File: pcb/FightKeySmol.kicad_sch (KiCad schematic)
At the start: 14 parts

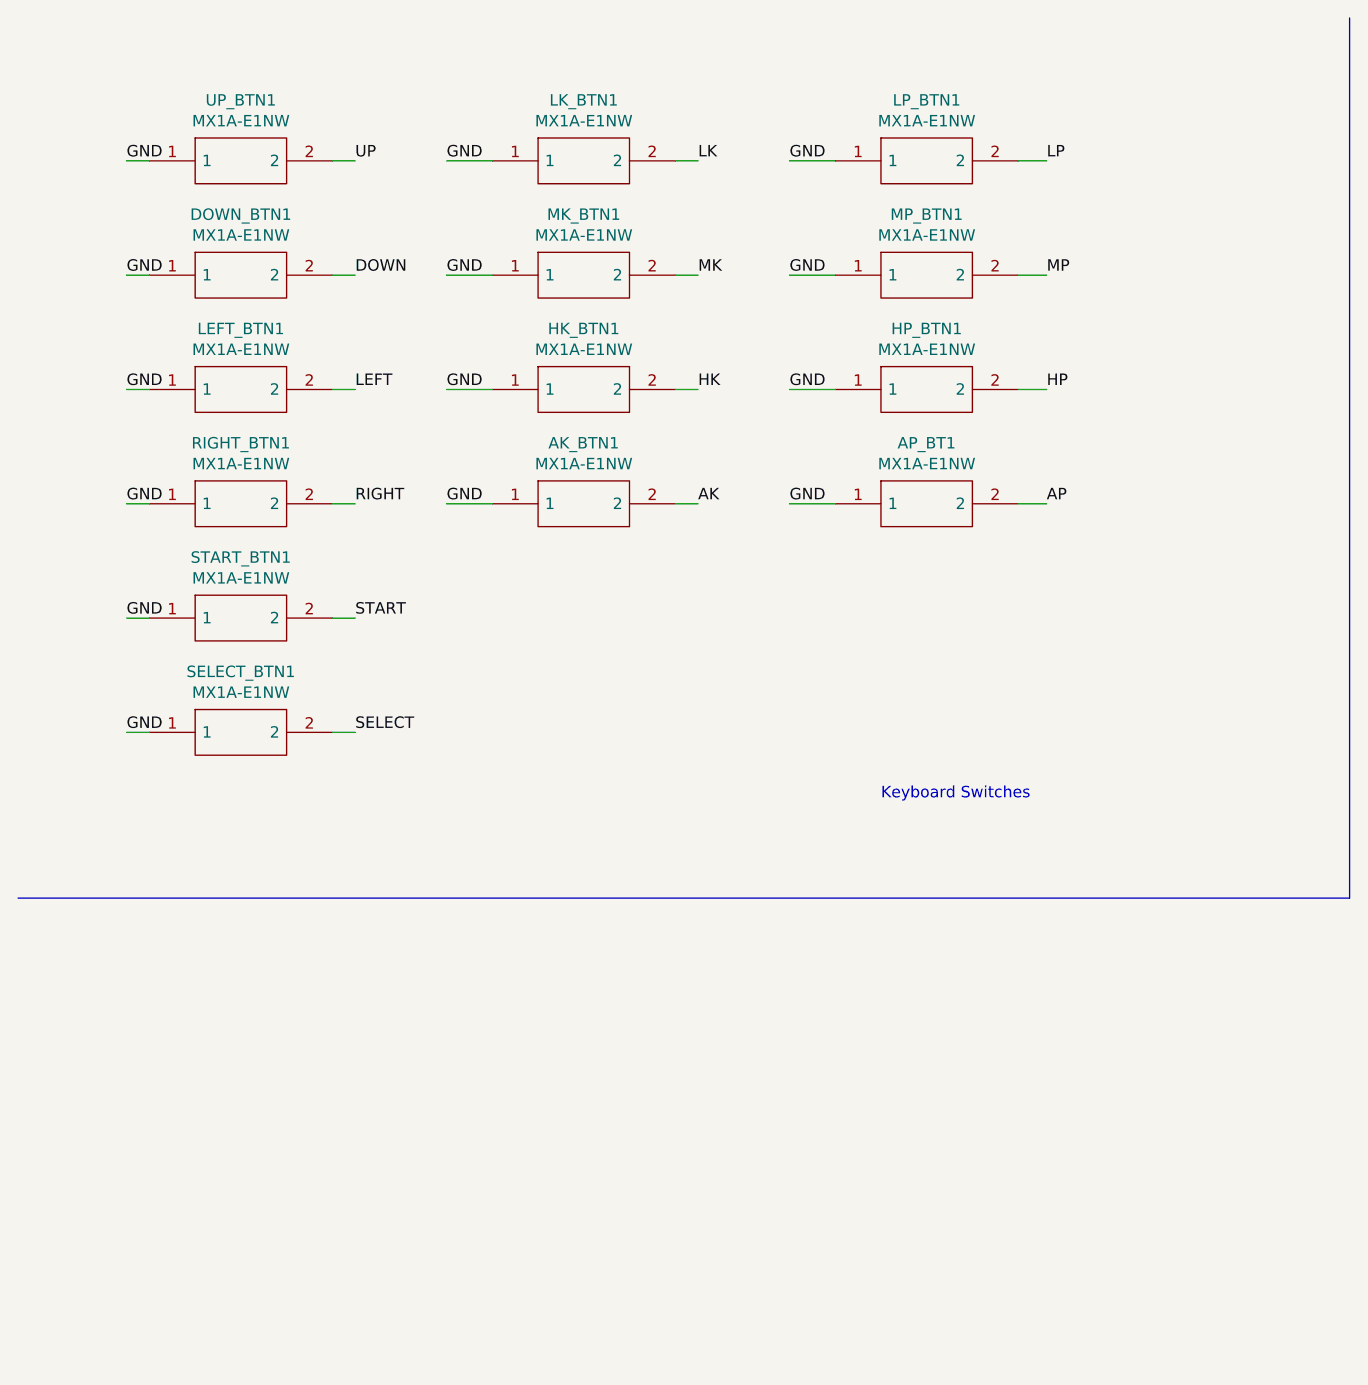
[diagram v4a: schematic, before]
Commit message: kicad_sch: implement USB/Power circuit
Signed-off-by: Dylan Turner <dylantdmt@gmail.com>
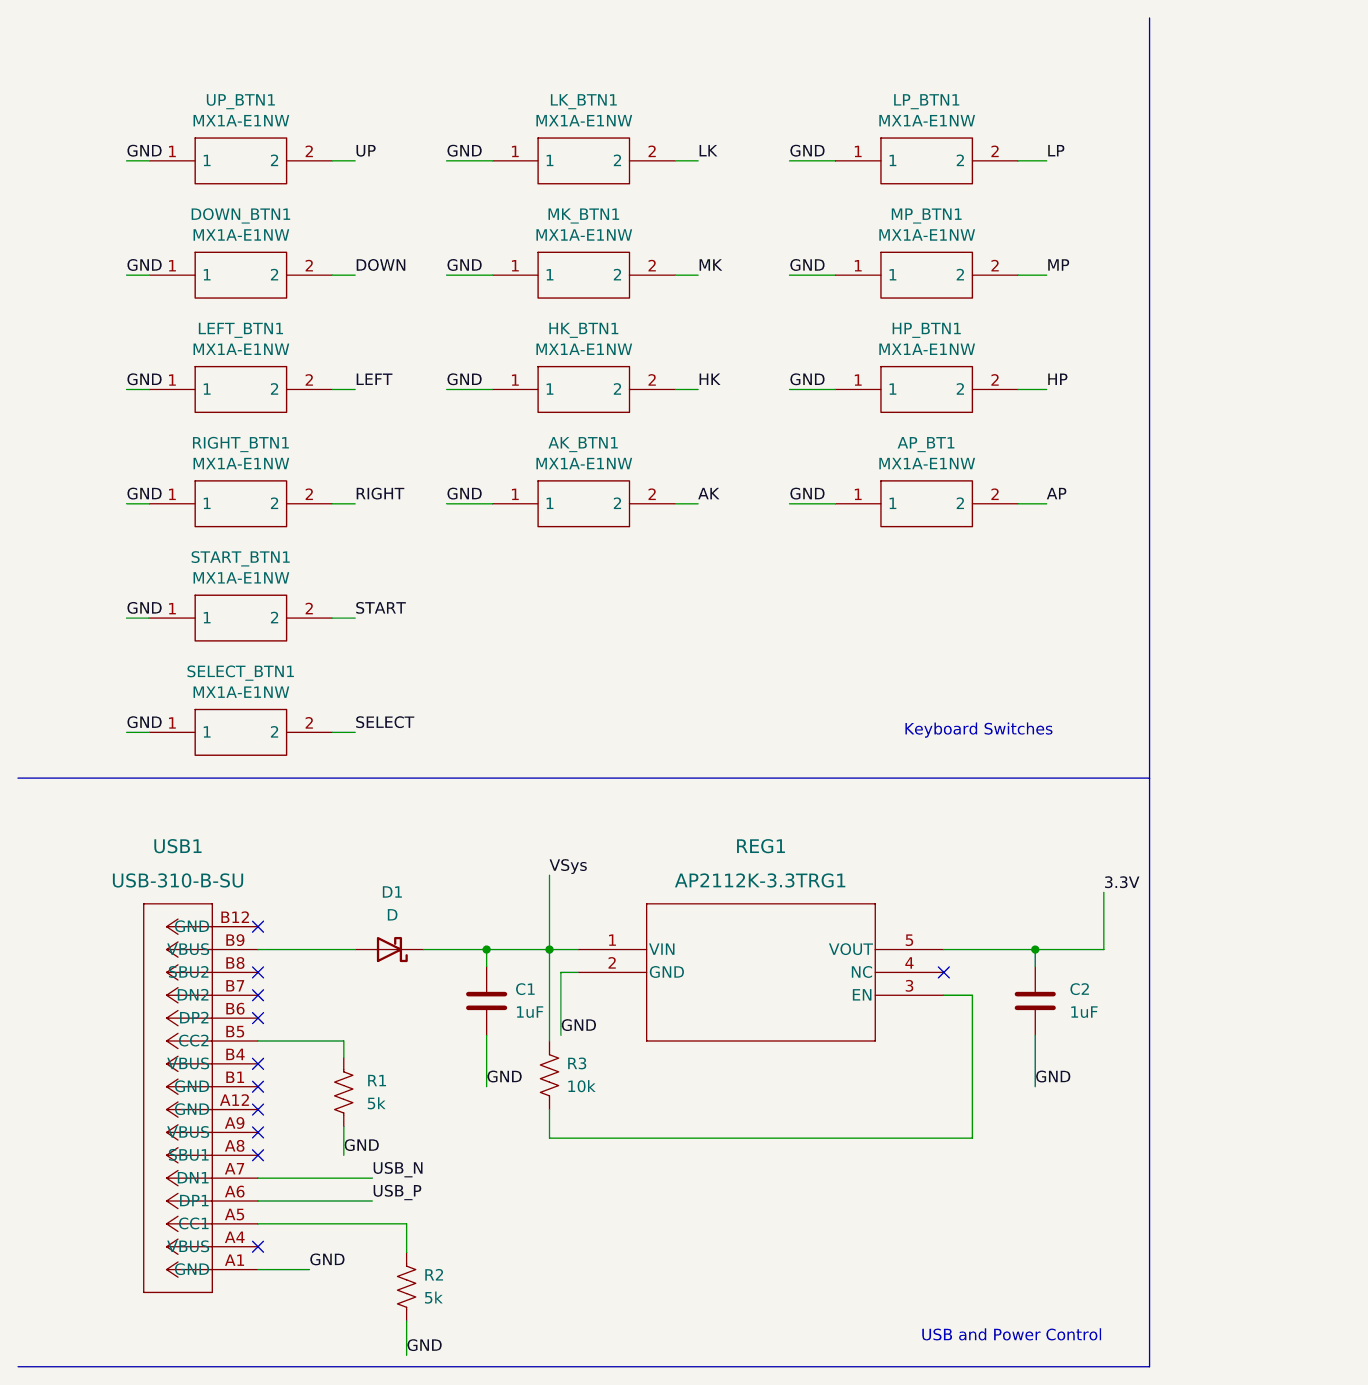
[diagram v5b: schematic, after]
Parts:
- added C1, C2: 1uF, Capacitor_SMD:C_1210_3225Metric, symbol Device:C
- added D1: D, Diode_SMD:D_SOD-323, symbol Device:D_Schottky
- added R1, R2: 5k, Resistor_SMD:R_0805_2012Metric, symbol Device:R_US
- added R3: 10k, Resistor_SMD:R_0201_0603Metric, symbol Device:R_US
- added REG1: AP2112K-3.3TRG1, SOT_RG1_DIO, symbol 3.3 Regulator:AP2112K-3.3TRG1
- added USB1: USB-310-B-SU, USB-C:CONN_USB-310-B-SU_HYA, symbol USB-C:USB-310-B-SU
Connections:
- net GND: now also C1.2, C2.2, R1.2, R2.2, REG1.2 (GND), USB1.A1 (GND)
- new net: D1.2 (A), USB1.B9 (VBUS)
- new net: R2.1, USB1.A5 (CC1)
- new net: R1.1, USB1.B5 (CC2)
- new net: R3.2, REG1.3 (EN)
- new net 3.3V: C2.1, REG1.5 (VOUT)
- new net USB_N: USB1.A7 (DN1)
- new net USB_P: USB1.A6 (DP1)
- new net VSys: C1.1, D1.1 (K), R3.1, REG1.1 (VIN)
- no-connect marks 0 -> 11
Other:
- note added: "USB and Power Control"

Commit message: kicad_sch: set up 2040 circuit
Signed-off-by: Dylan Turner <dylantdmt@gmail.com>
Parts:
- added C10, C11, C12, C13, C14, C5, C6, C7, C8, C9: 100nF, Capacitor_SMD:C_1210_3225Metric, symbol Device:C
- added C15, C16: 27pF, Capacitor_SMD:C_1210_3225Metric, symbol Device:C
- added C3, C4: 1uF, Capacitor_SMD:C_1210_3225Metric, symbol Device:C
- added R4, R7: 10k, Resistor_SMD:R_0201_0603Metric, symbol Device:R_US
- added R5, R6: 27, Resistor_SMD:R_1206_3216Metric, symbol Device:R_US
- added R8, R9: 1k, Resistor_SMD:R_0201_0603Metric, symbol Device:R_US
- added RDNP1: DNP, Resistor_SMD:R_0201_0603Metric, symbol Device:R_US
- added SW_BOOT1: SW_Push, Button_Switch_SMD:SW_SPST_PTS645, symbol Switch:SW_Push
- added U1: RP2040TR7, RP2040TR7_RPI, symbol RP2040:RP2040TR7
- added U2: W25Q32JVSSIQ, SOIC-8_5P28X5P28_WIN, symbol SPI Flash:W25Q32JVSSIQ
- added Y1: Crystal, Crystal:Crystal_SMD_HC49-SD, symbol Device:Crystal
- renumbered AP_BT1 to AP_BTN1
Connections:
- net 3.3V: now also C10.1, C11.1, C12.1, C4.1, C5.1, C6.1, C7.1, C8.1, C9.1, R4.1, R7.1, U1.1 (IOVDD), U1.10 (IOVDD), U1.22 (IOVDD), U1.33 (IOVDD), U1.42 (IOVDD), U1.43 (ADC_AVDD), U1.44 (VREG_VIN), U1.48 (USB_VDD), U1.49 (IOVDD), U2.8 (VCC)
- net GND: now also C10.2, C11.2, C12.2, C13.2, C14.2, C15.2, C16.2, C3.2, C4.2, C5.2, C6.2, C7.2, C8.2, C9.2, SW_BOOT1.2, U1.19 (TESTEN), U1.57 (EPAD), U2.4 (GND)
- net USB_N: now also R6.1
- net USB_P: now also R5.2
- new net: C16.1, R9.1, Y1.2
- new net: R4.2, U1.26 (RUN)
- new net: R6.2, U1.46 (USB_DM)
- new net: R5.1, U1.47 (USB_DP)
- new net 1.1V: C13.1, C14.1, C3.1, U1.23 (DVDD), U1.45 (VREG_VOUT), U1.50 (DVDD)
- new net AK_BTN1: U1.11 (GPIO8)
- new net AP_BTN1: U1.12 (GPIO9)
- new net DOWN_BTN1: U1.5 (GPIO3)
- new net HK_BTN1: U1.15 (GPIO12)
- new net HP_BTN1: U1.16 (GPIO13)
- new net LEFT_BTN1: U1.7 (GPIO5)
- new net LK_BTN1: U1.8 (GPIO6)
- new net LP_BTN1: U1.13 (GPIO10)
- new net MK_BTN1: U1.9 (GPIO7)
- new net MP_BTN1: U1.14 (GPIO11)
- new net QSPI_CS: R7.2, R8.2, U1.56 (QSPI_SS_N), U2.1 (/CS)
- new net QSPI_SCK: U1.52 (QSPI_SCLK), U2.6 (CLK)
- new net QSPI_SD0: U1.53 (QSPI_SD0), U2.5 (DI(IO0))
- new net QSPI_SD1: U1.55 (QSPI_SD1), U2.2 (DO(IO1))
- new net QSPI_SD2: U1.54 (QSPI_SD2), U2.3 (/WP(IO2))
- new net QSPI_SD3: U1.51 (QSPI_SD3), U2.7 (/HOLD_OR_/RESET(IO3))
- new net RIGHT_BTN1: U1.6 (GPIO4)
- new net SELECT_BTN1: U1.27 (GPIO16)
- new net START_BTN1: U1.28 (GPIO17)
- new net UP_BTN1: U1.4 (GPIO2)
- new net USB_BOOT: R8.1, SW_BOOT1.1
- new net XIN: C15.1, RDNP1.1, U1.20 (XIN), Y1.1
- new net XOUT: R9.2, RDNP1.2, U1.21 (XOUT)
- no-connect marks 11 -> 29
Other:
- note added: "Boot Select"
- note added: "Near ADC_AVDD"
- note added: "Near DVDD"
- note added: "Near IOVDD"
- note added: "RP2040"

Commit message: kicad_*: finished implementing custom 2040 circuit
Should work and should be able to be placed entirely by manufacturer

Signed-off-by: Dylan Turner <dylantdmt@gmail.com>
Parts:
- C1, C10, C11, C12, C13, C14, C15, C16, C2, C3, C4, C5, C6, C7, C8, C9: footprint Capacitor_SMD:C_1210_3225Metric -> Capacitor_SMD:C_0201_0603Metric
- R5, R6: footprint Resistor_SMD:R_1206_3216Metric -> Resistor_SMD:R_0201_0603Metric
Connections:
- net AK_BTN1 is gone; now on net AK: U1.11 (GPIO8)
- net AP_BTN1 is gone; now on net AP: U1.12 (GPIO9)
- net DOWN_BTN1 is gone; now on net DOWN: U1.5 (GPIO3)
- net HK_BTN1 is gone; now on net HK: U1.15 (GPIO12)
- net HP_BTN1 is gone; now on net HP: U1.16 (GPIO13)
- net LEFT_BTN1 is gone; now on net LEFT: U1.7 (GPIO5)
- net LK_BTN1 is gone; now on net LK: U1.8 (GPIO6)
- net LP_BTN1 is gone; now on net LP: U1.13 (GPIO10)
- net MK_BTN1 is gone; now on net MK: U1.9 (GPIO7)
- net MP_BTN1 is gone; now on net MP: U1.14 (GPIO11)
- net RIGHT_BTN1 is gone; now on net RIGHT: U1.6 (GPIO4)
- net SELECT_BTN1 is gone; now on net SELECT: U1.27 (GPIO16)
- net START_BTN1 is gone; now on net START: U1.28 (GPIO17)
- net UP_BTN1 is gone; now on net UP: U1.4 (GPIO2)
